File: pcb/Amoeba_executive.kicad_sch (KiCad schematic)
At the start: 4 parts, among them J1 Conn_01x04_MountingPin, J2 Conn_01x04_MountingPin, SW1 SW_PUSH_LED

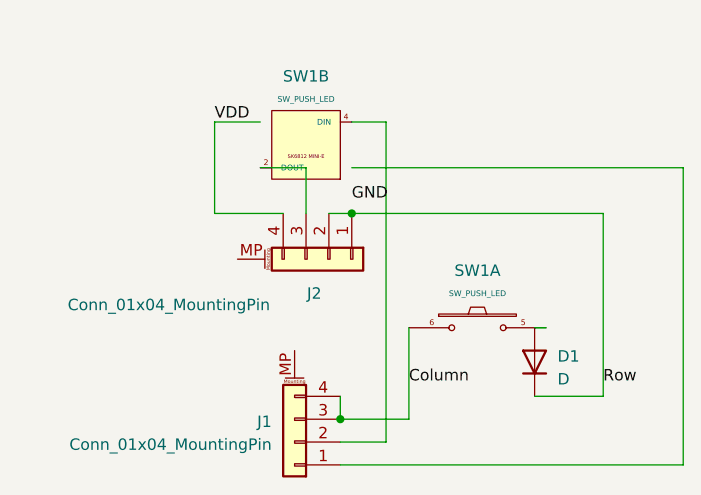
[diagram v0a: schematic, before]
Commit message: two sets of 5 pins
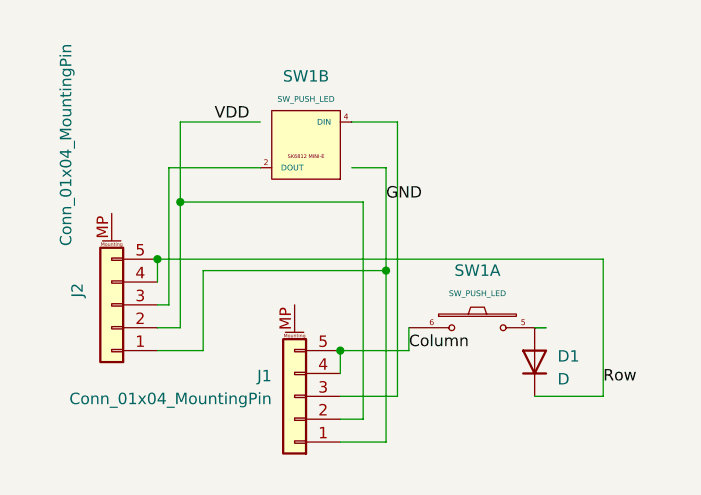
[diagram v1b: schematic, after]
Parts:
- J1, J2: footprint ergodonk_kicad_library:amoeba_executive_4pinn_conn -> ergodonk_kicad_library:amoeba_executive_5pinn_conn; symbol Connector_Generic_MountingPin:Conn_01x04_MountingPin -> Connector_Generic_MountingPin:Conn_01x05_MountingPin
- SW1: footprint ergodonk_kicad_library:amoeba_executive_V2 -> ergodonk_kicad_library:amoeba_executive_V4
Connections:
- net Column: now also J1.5 (Pin_5); no longer J1.3 (Pin_3)
- net GND: now also J2.1 (Pin_1)
- net Row: now also J2.4 (Pin_4), J2.5 (Pin_5); no longer J2.1 (Pin_1), J2.2 (Pin_2)
- net VDD: now also J1.2 (Pin_2), J2.2 (Pin_2); no longer J2.4 (Pin_4)
- net at SW1.4 (DIN): now also J1.3 (Pin_3); no longer J1.2 (Pin_2)
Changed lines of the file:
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@@
 (kicad_sch (version 20230121) (generator eeschema)
   (paper "A4")
-  (junction (at 129.54 52.07) (diameter 0) (color 0 0 0 0)
-  )
-  (junction (at 128.27 74.93) (diameter 0) (color 0 0 0 0)
-  )
-  (wire (pts (xy 124.46 46.99) (xy 119.38 46.99))
-    (stroke (width 0) (type default))
-  )
-  (wire (pts (xy 124.46 52.07) (xy 124.46 46.99))
+  (junction (at 128.27 67.31) (diameter 0) (color 0 0 0 0)
+  )
+  (junction (at 110.49 50.8) (diameter 0) (color 0 0 0 0)
+  )
+  (junction (at 133.35 58.42) (diameter 0) (color 0 0 0 0)
+  )
+  (junction (at 107.95 57.15) (diameter 0) (color 0 0 0 0)
+  )
+  (wire (pts (xy 133.35 77.47) (xy 128.27 77.47))
+    (stroke (width 0) (type default))
+  )
+  (wire (pts (xy 128.27 67.31) (xy 128.27 69.85))
     (stroke (width 0) (type default))
   )
@@
     (stroke (width 0) (type default))
   )
-  (wire (pts (xy 114.3 52.07) (xy 121.92 52.07))
-    (stroke (width 0) (type default))
-  )
-  (wire (pts (xy 157.48 72.39) (xy 157.48 52.07))
-    (stroke (width 0) (type default))
-  )
-  (wire (pts (xy 114.3 41.91) (xy 114.3 52.07))
-    (stroke (width 0) (type default))
-  )
-  (wire (pts (xy 129.54 41.91) (xy 133.35 41.91))
-    (stroke (width 0) (type default))
-  )
-  (wire (pts (xy 119.38 41.91) (xy 114.3 41.91))
-    (stroke (width 0) (type default))
-  )
-  (wire (pts (xy 166.37 46.99) (xy 166.37 80.01))
+  (wire (pts (xy 109.22 62.23) (xy 107.95 62.23))
+    (stroke (width 0) (type default))
+  )
+  (wire (pts (xy 113.03 58.42) (xy 133.35 58.42))
+    (stroke (width 0) (type default))
+  )
+  (wire (pts (xy 110.49 50.8) (xy 110.49 64.77))
+    (stroke (width 0) (type default))
+  )
+  (wire (pts (xy 157.48 72.39) (xy 157.48 57.15))
+    (stroke (width 0) (type default))
+  )
+  (wire (pts (xy 109.22 46.99) (xy 109.22 62.23))
+    (stroke (width 0) (type default))
+  )
+  (wire (pts (xy 134.62 41.91) (xy 134.62 72.39))
+    (stroke (width 0) (type default))
+  )
+  (wire (pts (xy 119.38 46.99) (xy 109.22 46.99))
+    (stroke (width 0) (type default))
+  )
+  (wire (pts (xy 110.49 41.91) (xy 119.38 41.91))
     (stroke (width 0) (type default))
   )
@@
     (stroke (width 0) (type default))
   )
-  (wire (pts (xy 133.35 41.91) (xy 133.35 77.47))
-    (stroke (width 0) (type default))
-  )
-  (wire (pts (xy 128.27 74.93) (xy 135.89 74.93))
-    (stroke (width 0) (type default))
-  )
-  (wire (pts (xy 127 52.07) (xy 129.54 52.07))
-    (stroke (width 0) (type default))
-  )
-  (wire (pts (xy 128.27 72.39) (xy 128.27 74.93))
-    (stroke (width 0) (type default))
-  )
-  (wire (pts (xy 166.37 80.01) (xy 128.27 80.01))
-    (stroke (width 0) (type default))
-  )
-  (wire (pts (xy 157.48 52.07) (xy 129.54 52.07))
-    (stroke (width 0) (type default))
-  )
-  (wire (pts (xy 129.54 46.99) (xy 166.37 46.99))
-    (stroke (width 0) (type default))
-  )
-  (wire (pts (xy 135.89 64.77) (xy 135.89 74.93))
-    (stroke (width 0) (type default))
-  )
-  (wire (pts (xy 133.35 77.47) (xy 128.27 77.47))
-    (stroke (width 0) (type default))
-  )
-  (label "Column" (at 135.89 71.12 0) (fields_autoplaced)
+  (wire (pts (xy 134.62 72.39) (xy 128.27 72.39))
+    (stroke (width 0) (type default))
+  )
+  (wire (pts (xy 130.81 74.93) (xy 128.27 74.93))
+    (stroke (width 0) (type default))
+  )
+  (wire (pts (xy 110.49 50.8) (xy 130.81 50.8))
+    (stroke (width 0) (type default))
+  )
+  (wire (pts (xy 107.95 57.15) (xy 157.48 57.15))
+    (stroke (width 0) (type default))
+  )
+  (wire (pts (xy 110.49 64.77) (xy 107.95 64.77))
+    (stroke (width 0) (type default))
+  )
+  (wire (pts (xy 107.95 57.15) (xy 107.95 59.69))
+    (stroke (width 0) (type default))
+  )
+  (wire (pts (xy 110.49 41.91) (xy 110.49 50.8))
+    (stroke (width 0) (type default))
+  )
+  (wire (pts (xy 113.03 67.31) (xy 113.03 58.42))
+    (stroke (width 0) (type default))
+  )
+  (wire (pts (xy 130.81 50.8) (xy 130.81 74.93))
+    (stroke (width 0) (type default))
+  )
+  (wire (pts (xy 133.35 58.42) (xy 133.35 77.47))
+    (stroke (width 0) (type default))
+  )
+  (wire (pts (xy 129.54 41.91) (xy 134.62 41.91))
+    (stroke (width 0) (type default))
+  )
+  (wire (pts (xy 133.35 46.99) (xy 129.54 46.99))
+    (stroke (width 0) (type default))
+  )
+  (wire (pts (xy 107.95 67.31) (xy 113.03 67.31))
+    (stroke (width 0) (type default))
+  )
+  (wire (pts (xy 135.89 64.77) (xy 135.89 67.31))
+    (stroke (width 0) (type default))
+  )
+  (wire (pts (xy 133.35 46.99) (xy 133.35 58.42))
+    (stroke (width 0) (type default))
+  )
+  (wire (pts (xy 128.27 67.31) (xy 135.89 67.31))
+    (stroke (width 0) (type default))
+  )
+  (label "Column" (at 135.89 67.31 0) (fields_autoplaced)
     (effects (font (size 1.27 1.27)) (justify left bottom))
   )
@@
     (effects (font (size 1.27 1.27)) (justify left bottom))
   )
-  (label "GND" (at 129.54 50.8 0) (fields_autoplaced)
+  (label "GND" (at 133.35 50.8 0) (fields_autoplaced)
     (effects (font (size 1.27 1.27)) (justify left bottom))
   )
@@
     (effects (font (size 1.27 1.27)) (justify left bottom))
   )
-  (symbol (lib_id "Connector_Generic_MountingPin:Conn_01x04_MountingPin") (at 123.19 77.47 180) (unit 1)
-    (in_bom yes) (on_board yes) (dnp no)
-    (property "Reference" "J1" (at 120.65 75.2094 0)
+  (symbol (lib_id "Connector_Generic_MountingPin:Conn_01x05_MountingPin") (at 123.19 72.39 180) (unit 1)
+    (in_bom yes) (on_board yes) (dnp no)
+    (property "Reference" "J1" (at 120.65 70.1294 0)
       (effects (font (size 1.27 1.27)) (justify left))
     )
-    (property "Value" "Conn_01x04_MountingPin" (at 120.65 77.7494 0)
+    (property "Value" "Conn_01x04_MountingPin" (at 120.65 72.6694 0)
       (effects (font (size 1.27 1.27)) (justify left))
     )
-    (property "Footprint" "ergodonk_kicad_library:amoeba_executive_4pinn_conn" (at 123.19 77.47 0)
-      (effects (font (size 1.27 1.27)) hide)
-    )
-    (property "Datasheet" "~" (at 123.19 77.47 0)
+    (property "Footprint" "ergodonk_kicad_library:amoeba_executive_5pinn_conn" (at 123.19 72.39 0)
+      (effects (font (size 1.27 1.27)) hide)
+    )
+    (property "Datasheet" "~" (at 123.19 72.39 0)
       (effects (font (size 1.27 1.27)) hide)
     )
@@
     (pin "3")
     (pin "4")
+    (pin "5")
     (pin "MP")
     (instances
@@
     )
   )
-  (symbol (lib_id "Connector_Generic_MountingPin:Conn_01x04_MountingPin") (at 127 57.15 270) (unit 1)
-    (in_bom yes) (on_board yes) (dnp no)
-    (property "Reference" "J2" (at 125.3744 60.96 90)
-      (effects (font (size 1.27 1.27)))
-    )
-    (property "Value" "Conn_01x04_MountingPin" (at 109.22 62.23 90)
-      (effects (font (size 1.27 1.27)))
-    )
-    (property "Footprint" "ergodonk_kicad_library:amoeba_executive_4pinn_conn" (at 127 57.15 0)
-      (effects (font (size 1.27 1.27)) hide)
-    )
-    (property "Datasheet" "~" (at 127 57.15 0)
+  (symbol (lib_id "Connector_Generic_MountingPin:Conn_01x05_MountingPin") (at 102.87 62.23 180) (unit 1)
+    (in_bom yes) (on_board yes) (dnp no)
+    (property "Reference" "J2" (at 99.06 60.6044 90)
+      (effects (font (size 1.27 1.27)))
+    )
+    (property "Value" "Conn_01x04_MountingPin" (at 97.79 44.45 90)
+      (effects (font (size 1.27 1.27)))
+    )
+    (property "Footprint" "ergodonk_kicad_library:amoeba_executive_5pinn_conn" (at 102.87 62.23 0)
+      (effects (font (size 1.27 1.27)) hide)
+    )
+    (property "Datasheet" "~" (at 102.87 62.23 0)
       (effects (font (size 1.27 1.27)) hide)
     )
@@
     (pin "3")
     (pin "4")
+    (pin "5")
     (pin "MP")
     (instances
@@
       (effects (font (size 0.635 0.635)))
     )
-    (property "Footprint" "ergodonk_kicad_library:amoeba_executive_V2" (at 125.222 39.37 0)
+    (property "Footprint" "ergodonk_kicad_library:amoeba_executive_V4" (at 125.222 39.37 0)
       (effects (font (size 1.27 1.27)) hide)
     )
@@
       (effects (font (size 0.635 0.635)))
     )
-    (property "Footprint" "ergodonk_kicad_library:amoeba_executive_V2" (at 144.272 59.69 0)
-      (effects (font (size 1.27 1.27)) hide)
-    )
+    (property "Footprint" "ergodonk_kicad_library:amoeba_executive_V4" (at 144.272 59.69 0)
+      (effects (font (size 1.27 1.27)) hide)
+    )

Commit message: First draft complete
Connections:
- net Row: now also D1.2 (A); no longer D1.1 (K)
- net at SW1.5: now also D1.1 (K); no longer D1.2 (A)
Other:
- moved on the sheet: D1
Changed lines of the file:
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@@
     (stroke (width 0) (type default))
   )
-  (wire (pts (xy 149.86 72.39) (xy 157.48 72.39))
+  (wire (pts (xy 151.13 72.39) (xy 157.48 72.39))
     (stroke (width 0) (type default))
   )
@@
   )
   (wire (pts (xy 110.49 41.91) (xy 119.38 41.91))
-    (stroke (width 0) (type default))
-  )
-  (wire (pts (xy 151.13 64.77) (xy 149.86 64.77))
     (stroke (width 0) (type default))
   )
@@
     )
   )
-  (symbol (lib_id "Device:D") (at 149.86 68.58 90) (unit 1)
+  (symbol (lib_id "Device:D") (at 151.13 68.58 270) (unit 1)
     (in_bom yes) (on_board yes) (dnp no)
-    (property "Reference" "D1" (at 152.4 67.945 90)
+    (property "Reference" "D1" (at 148.59 69.215 90)
       (effects (font (size 1.27 1.27)) (justify right))
     )
-    (property "Value" "D" (at 152.4 70.485 90)
+    (property "Value" "D" (at 148.59 66.675 90)
       (effects (font (size 1.27 1.27)) (justify right))
     )
-    (property "Footprint" "ergodonk_kicad_library:D_SOD-123_DO-35_Hybrid_DoubleSided" (at 149.86 68.58 0)
+    (property "Footprint" "ergodonk_kicad_library:D_SOD-123_DO-35_Hybrid_DoubleSided" (at 151.13 68.58 0)
       (effects (font (size 1.27 1.27)) hide)
     )
-    (property "Datasheet" "~" (at 149.86 68.58 0)
+    (property "Datasheet" "~" (at 151.13 68.58 0)
       (effects (font (size 1.27 1.27)) hide)
     )
-    (property "Sim.Device" "D" (at 149.86 68.58 0)
+    (property "Sim.Device" "D" (at 151.13 68.58 0)
       (effects (font (size 1.27 1.27)) hide)
     )
-    (property "Sim.Pins" "1=K 2=A" (at 149.86 68.58 0)
+    (property "Sim.Pins" "1=K 2=A" (at 151.13 68.58 0)
       (effects (font (size 1.27 1.27)) hide)
     )

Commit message: Created footprint library consolidated footprints in new library adjusted pads for single sided diodes
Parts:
- D1: footprint ergodonk_kicad_library:D_SOD-123_DO-35_Hybrid_DoubleSided -> Amoeba_executive_footprints:D_SOD-123_DO-35_Hybrid_Single_sided
- J1, J2: footprint ergodonk_kicad_library:amoeba_executive_5pinn_conn -> Amoeba_executive_footprints:amoeba_executive_5pinn_conn
- SW1: footprint ergodonk_kicad_library:amoeba_executive_V4 -> Amoeba_executive_footprints:amoeba_executive_V4
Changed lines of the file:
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@@
       (effects (font (size 1.27 1.27)) (justify left))
     )
-    (property "Footprint" "ergodonk_kicad_library:amoeba_executive_5pinn_conn" (at 123.19 72.39 0)
+    (property "Footprint" "Amoeba_executive_footprints:amoeba_executive_5pinn_conn" (at 123.19 72.39 0)
       (effects (font (size 1.27 1.27)) hide)
     )
@@
       (effects (font (size 1.27 1.27)))
     )
-    (property "Footprint" "ergodonk_kicad_library:amoeba_executive_5pinn_conn" (at 102.87 62.23 0)
+    (property "Footprint" "Amoeba_executive_footprints:amoeba_executive_5pinn_conn" (at 102.87 62.23 0)
       (effects (font (size 1.27 1.27)) hide)
     )
@@
       (effects (font (size 1.27 1.27)) (justify right))
     )
-    (property "Footprint" "ergodonk_kicad_library:D_SOD-123_DO-35_Hybrid_DoubleSided" (at 151.13 68.58 0)
+    (property "Footprint" "Amoeba_executive_footprints:D_SOD-123_DO-35_Hybrid_Single_sided" (at 151.13 68.58 0)
       (effects (font (size 1.27 1.27)) hide)
     )
@@
       (effects (font (size 0.635 0.635)))
     )
-    (property "Footprint" "ergodonk_kicad_library:amoeba_executive_V4" (at 125.222 39.37 0)
+    (property "Footprint" "Amoeba_executive_footprints:amoeba_executive_V4" (at 125.222 39.37 0)
       (effects (font (size 1.27 1.27)) hide)
     )
@@
       (effects (font (size 0.635 0.635)))
     )
-    (property "Footprint" "ergodonk_kicad_library:amoeba_executive_V4" (at 144.272 59.69 0)
+    (property "Footprint" "Amoeba_executive_footprints:amoeba_executive_V4" (at 144.272 59.69 0)
       (effects (font (size 1.27 1.27)) hide)
     )
